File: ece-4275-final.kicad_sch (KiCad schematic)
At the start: 0 parts

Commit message: add esp32-s3
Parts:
- added U1: ESP32-S3, Package_DFN_QFN:QFN-56-1EP_7x7mm_P0.4mm_EP4x4mm, symbol MCU_Espressif:ESP32-S3
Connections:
- new net: U1.2 (VDD3P3), U1.3 (VDD3P3)
- new net: U1.55 (VDDA), U1.56 (VDDA)
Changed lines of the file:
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@@
 	(generator_version "10.0")
 	(paper "A4")
+	(symbol
+		(lib_id "MCU_Espressif:ESP32-S3")
+		(at 144.78 90.17 0)
+		(unit 1)
+		(body_style 1)
+		(exclude_from_sim no)
+		(in_bom yes)
+		(on_board yes)
+		(in_pos_files yes)
+		(dnp no)
+		(fields_autoplaced yes)
+		(property "Reference" "U1"
+			(at 146.9233 128.27 0)
+			(show_name no)
+			(do_not_autoplace no)
+			(effects
+				(font
+					(size 1.27 1.27)
+				)
+				(justify left)
+			)
+		)
+		(property "Value" "ESP32-S3"
+			(at 146.9233 130.81 0)
+			(show_name no)
+			(do_not_autoplace no)
+			(effects
+				(font
+					(size 1.27 1.27)
+				)
+				(justify left)
+			)
+		)
+		(property "Footprint" "Package_DFN_QFN:QFN-56-1EP_7x7mm_P0.4mm_EP4x4mm"
+			(at 144.78 138.43 0)
+			(hide yes)
+			(show_name no)
+			(do_not_autoplace no)
+			(effects
+				(font
+					(size 1.27 1.27)
+				)
+			)
+		)
+		(property "Datasheet" "https://www.espressif.com/sites/default/files/documentation/esp32-s3_datasheet_en.pdf"
+			(at 144.78 90.17 0)
+			(hide yes)
+			(show_name no)
+			(do_not_autoplace no)
+			(effects
+				(font
+					(size 1.27 1.27)
+				)
+			)
+		)
+		(property "Description" "Microcontroller, Wi-Fi 802.11b/g/n, Bluetooth, 32bit"
+			(at 144.78 90.17 0)
+			(hide yes)
+			(show_name no)
+			(do_not_autoplace no)
+			(effects
+				(font
+					(size 1.27 1.27)
+				)
+			)
+		)
+		(pin "57"
+		)
+		(pin "55"
+		)
+		(pin "54"
+		)
+		(pin "53"
+		)
+		(pin "52"
+		)
+		(pin "50"
+		)
+		(pin "49"
+		)
+		(pin "48"
+		)
+		(pin "47"
+		)
+		(pin "46"
+		)
+		(pin "44"
+		)
+		(pin "43"
+		)
+		(pin "42"
+		)
+		(pin "41"
+		)
+		(pin "40"
+		)
+		(pin "39"
+		)
+		(pin "38"
+		)
+		(pin "37"
+		)
+		(pin "35"
+		)
+		(pin "34"
+		)
+		(pin "27"
+		)
+		(pin "28"
+		)
+		(pin "29"
+		)
+		(pin "30"
+		)
+		(pin "31"
+		)
+		(pin "32"
+		)
+		(pin "33"
+		)
+		(pin "4"
+		)
+		(pin "5"
+		)
+		(pin "6"
+		)
+		(pin "7"
+		)
+		(pin "8"
+		)
+		(pin "9"
+		)
+		(pin "10"
+		)
+		(pin "11"
+		)
+		(pin "12"
+		)
+		(pin "13"
+		)
+		(pin "14"
+		)
+		(pin "15"
+		)
+		(pin "16"
+		)
+		(pin "17"
+		)
+		(pin "18"
+		)
+		(pin "19"
+		)
+		(pin "20"
+		)
+		(pin "21"
+		)
+		(pin "22"
+		)
+		(pin "23"
+		)
+		(pin "24"
+		)
+		(pin "25"
+		)
+		(pin "26"
+		)
+		(pin "1"
+		)
+		(pin "2"
+		)
+		(pin "3"
+		)
+		(pin "36"
+		)
+		(pin "45"
+		)
+		(pin "51"
+		)
+		(pin "56"
+		)
+		(instances
+			(project "ece-4275-final"
+				(path "/0c77f2af-cddb-472c-9a1b-8caed066380b"
+					(reference "U1")
+					(unit 1)
+				)
+			)
+		)
+	)
 	(sheet_instances
 		(path "/"

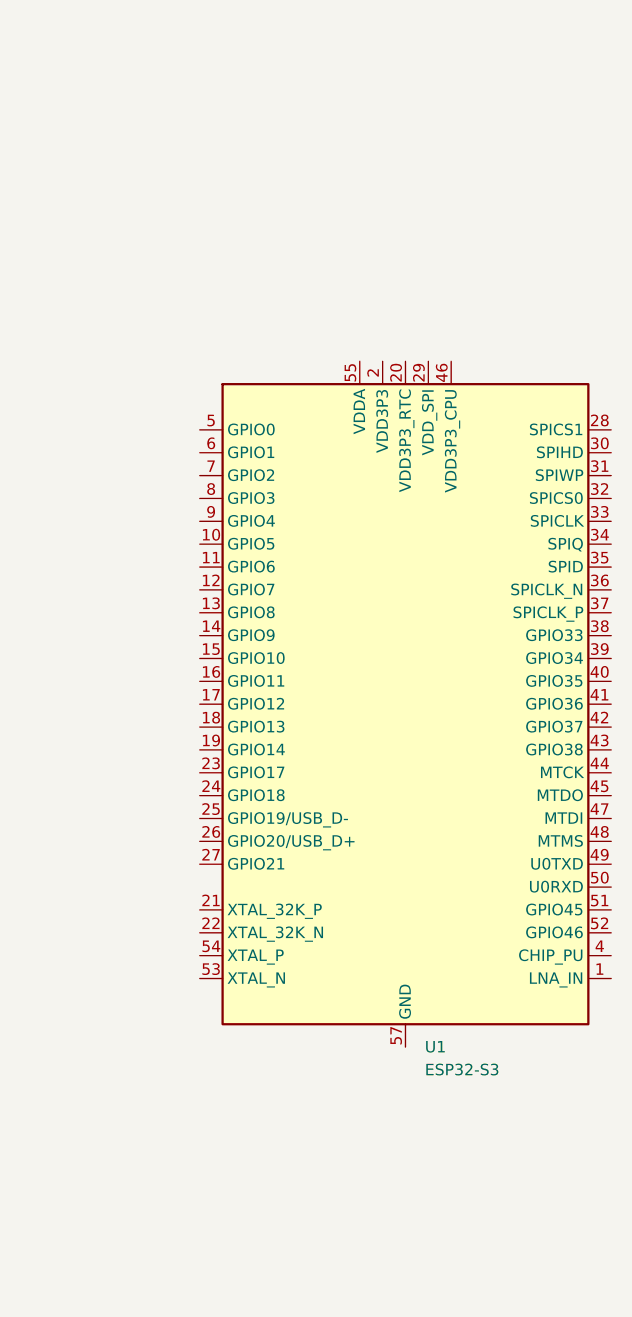
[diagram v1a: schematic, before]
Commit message: add dc step down
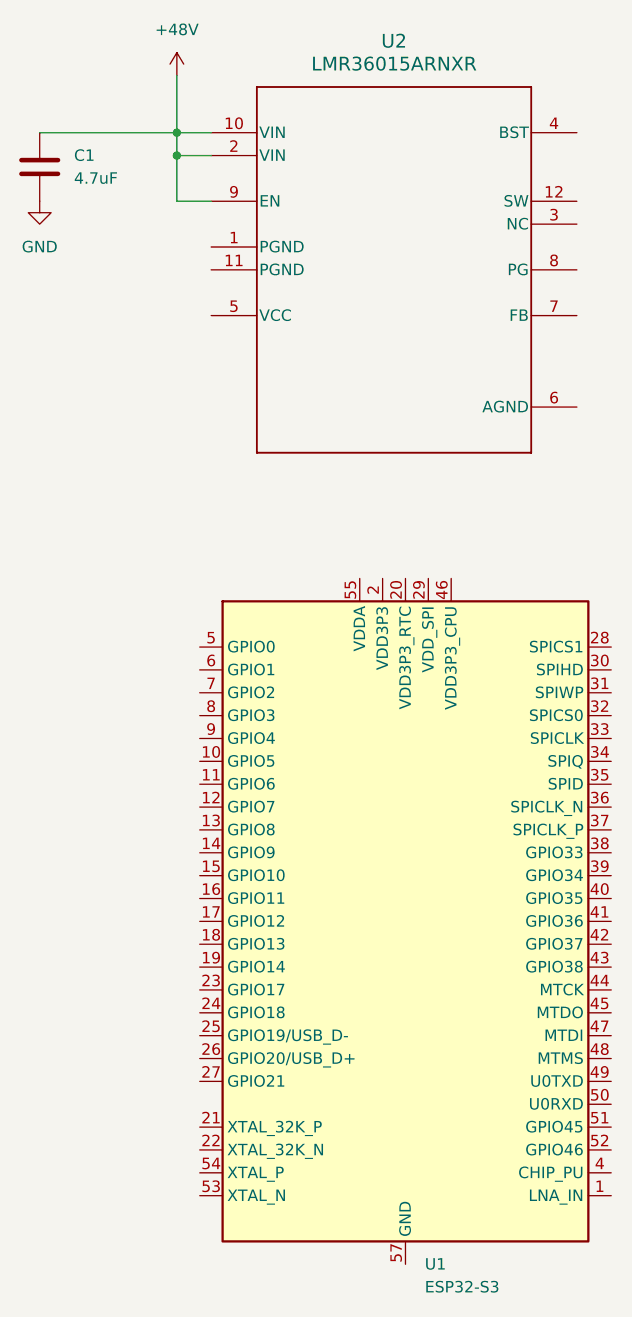
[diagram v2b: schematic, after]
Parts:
- added C1: 4.7uF, symbol Device:C
- added U2: LMR36015ARNXR, RNX0012B, symbol 2026-04-16_22-04-10:LMR36015ARNXR
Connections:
- new net +48V: C1.1, U2.10 (VIN), U2.2 (VIN), U2.9 (EN)
- new net GND: C1.2
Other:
- moved on the sheet: U1

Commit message: add library for local imports
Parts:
- removed U2: LMR36015ARNXR, RNX0012B, symbol 2026-04-16_22-04-10:LMR36015ARNXR
- added U2: LMR36015ARNXR, IMPORTS:LMR36015, symbol IMPORTS:LMR36015ARNXR
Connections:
- net +48V: now also U2.10 (VIN), U2.2 (VIN), U2.9 (EN)
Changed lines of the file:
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@@
-	)
-	(symbol
-		(lib_id "2026-04-16_22-04-10:LMR36015ARNXR")
-		(at 143.51 41.91 0)
-		(unit 1)
-		(body_style 1)
-		(exclude_from_sim no)
-		(in_bom yes)
-		(on_board yes)
-		(in_pos_files yes)
-		(dnp no)
-		(fields_autoplaced yes)
-		(property "Reference" "U2"
-			(at 143.51 16.51 0)
-			(show_name no)
-			(do_not_autoplace no)
-			(effects
-				(font
-					(size 1.524 1.524)
-				)
-			)
-		)
-		(property "Value" "LMR36015ARNXR"
-			(at 143.51 19.05 0)
-			(show_name no)
-			(do_not_autoplace no)
-			(effects
-				(font
-					(size 1.524 1.524)
-				)
-			)
-		)
-		(property "Footprint" "RNX0012B"
-			(at 143.51 41.91 0)
-			(hide yes)
-			(show_name no)
-			(do_not_autoplace no)
-			(effects
-				(font
-					(size 1.27 1.27)
-					(italic yes)
-				)
-			)
-		)
-		(property "Datasheet" "https://www.ti.com/lit/gpn/lmr36015"
-			(at 143.51 41.91 0)
-			(hide yes)
-			(show_name no)
-			(do_not_autoplace no)
-			(effects
-				(font
-					(size 1.27 1.27)
-					(italic yes)
-				)
-			)
-		)
-		(property "Description" ""
-			(at 143.51 41.91 0)
-			(hide yes)
-			(show_name no)
-			(do_not_autoplace no)
-			(effects
-				(font
-					(size 1.27 1.27)
-				)
-			)
-		)
-		(pin "2"
-		)
-		(pin "1"
-		)
-		(pin "12"
-		)
-		(pin "11"
-		)
-		(pin "10"
-		)
-		(pin "9"
-		)
-		(pin "8"
-		)
-		(pin "7"
-		)
-		(pin "6"
-		)
-		(pin "5"
-		)
-		(pin "4"
-		)
-		(pin "3"
-		)
-		(instances
-			(project "ece-4275-final"
-				(path "/0c77f2af-cddb-472c-9a1b-8caed066380b"
-					(reference "U2")
-					(unit 1)
-				)
-			)
-		)
 	)
 	(symbol
@@
 					(unit 1)
 				)
+			)
+		)
+	)
+	(symbol
+		(lib_id "IMPORTS:LMR36015ARNXR")
+		(at 143.51 41.91 0)
+		(unit 1)
+		(body_style 1)
+		(exclude_from_sim no)
+		(in_bom yes)
+		(on_board yes)
+		(in_pos_files yes)
+		(dnp no)
+		(fields_autoplaced yes)
+		(property "Reference" "U2"
+			(at 143.51 16.51 0)
+			(show_name no)
+			(do_not_autoplace no)
+			(effects
+				(font
+					(size 1.524 1.524)
+				)
+			)
+		)
+		(property "Value" "LMR36015ARNXR"
+			(at 143.51 19.05 0)
+			(show_name no)
+			(do_not_autoplace no)
+			(effects
+				(font
+					(size 1.524 1.524)
+				)
+			)
+		)
+		(property "Footprint" "IMPORTS:LMR36015"
+			(at 143.51 41.91 0)
+			(hide yes)
+			(show_name no)
+			(do_not_autoplace no)
+			(effects
+				(font
+					(size 1.27 1.27)
+					(italic yes)
+				)
+			)
+		)
+		(property "Datasheet" "https://www.ti.com/lit/gpn/lmr36015"
+			(at 143.51 41.91 0)
+			(hide yes)
+			(show_name no)
+			(do_not_autoplace no)
+			(effects
+				(font
+					(size 1.27 1.27)
+					(italic yes)
+				)
+			)
+		)
+		(property "Description" ""
+			(at 143.51 41.91 0)
+			(hide yes)
+			(show_name no)
+			(do_not_autoplace no)
+			(effects
+				(font
+					(size 1.27 1.27)
+				)
+			)
+		)
+		(pin "6"
+		)
+		(pin "5"
+		)
+		(pin "2"
+		)
+		(pin "4"
+		)
+		(pin "1"
+		)
+		(pin "3"
+		)
+		(pin "11"
+		)
+		(pin "10"
+		)
+		(pin "12"
+		)
+		(pin "9"
+		)
+		(pin "8"
+		)
+		(pin "7"
+		)
+		(instances
+			(project "ece-4275-final"
+				(path "/0c77f2af-cddb-472c-9a1b-8caed066380b"
+					(reference "U2")
+					(unit 1)
+				)

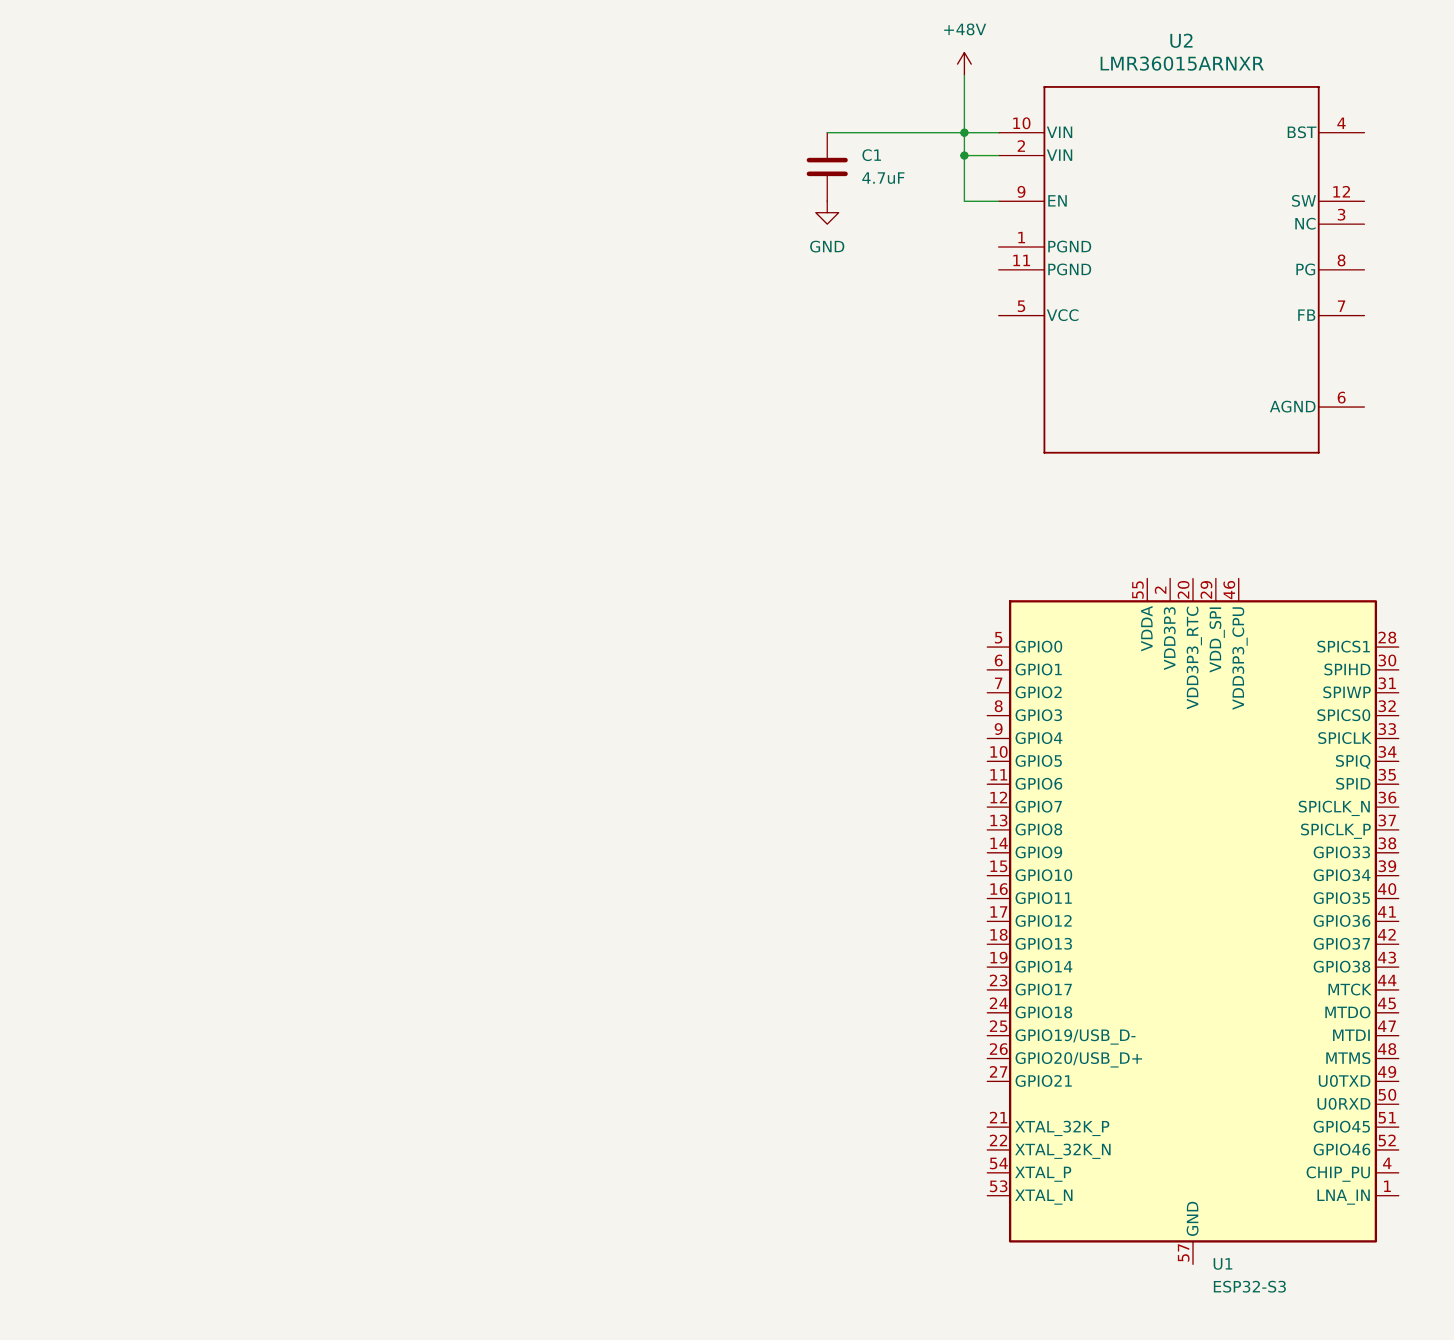
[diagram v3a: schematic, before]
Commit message: add DCDC converter + LDO
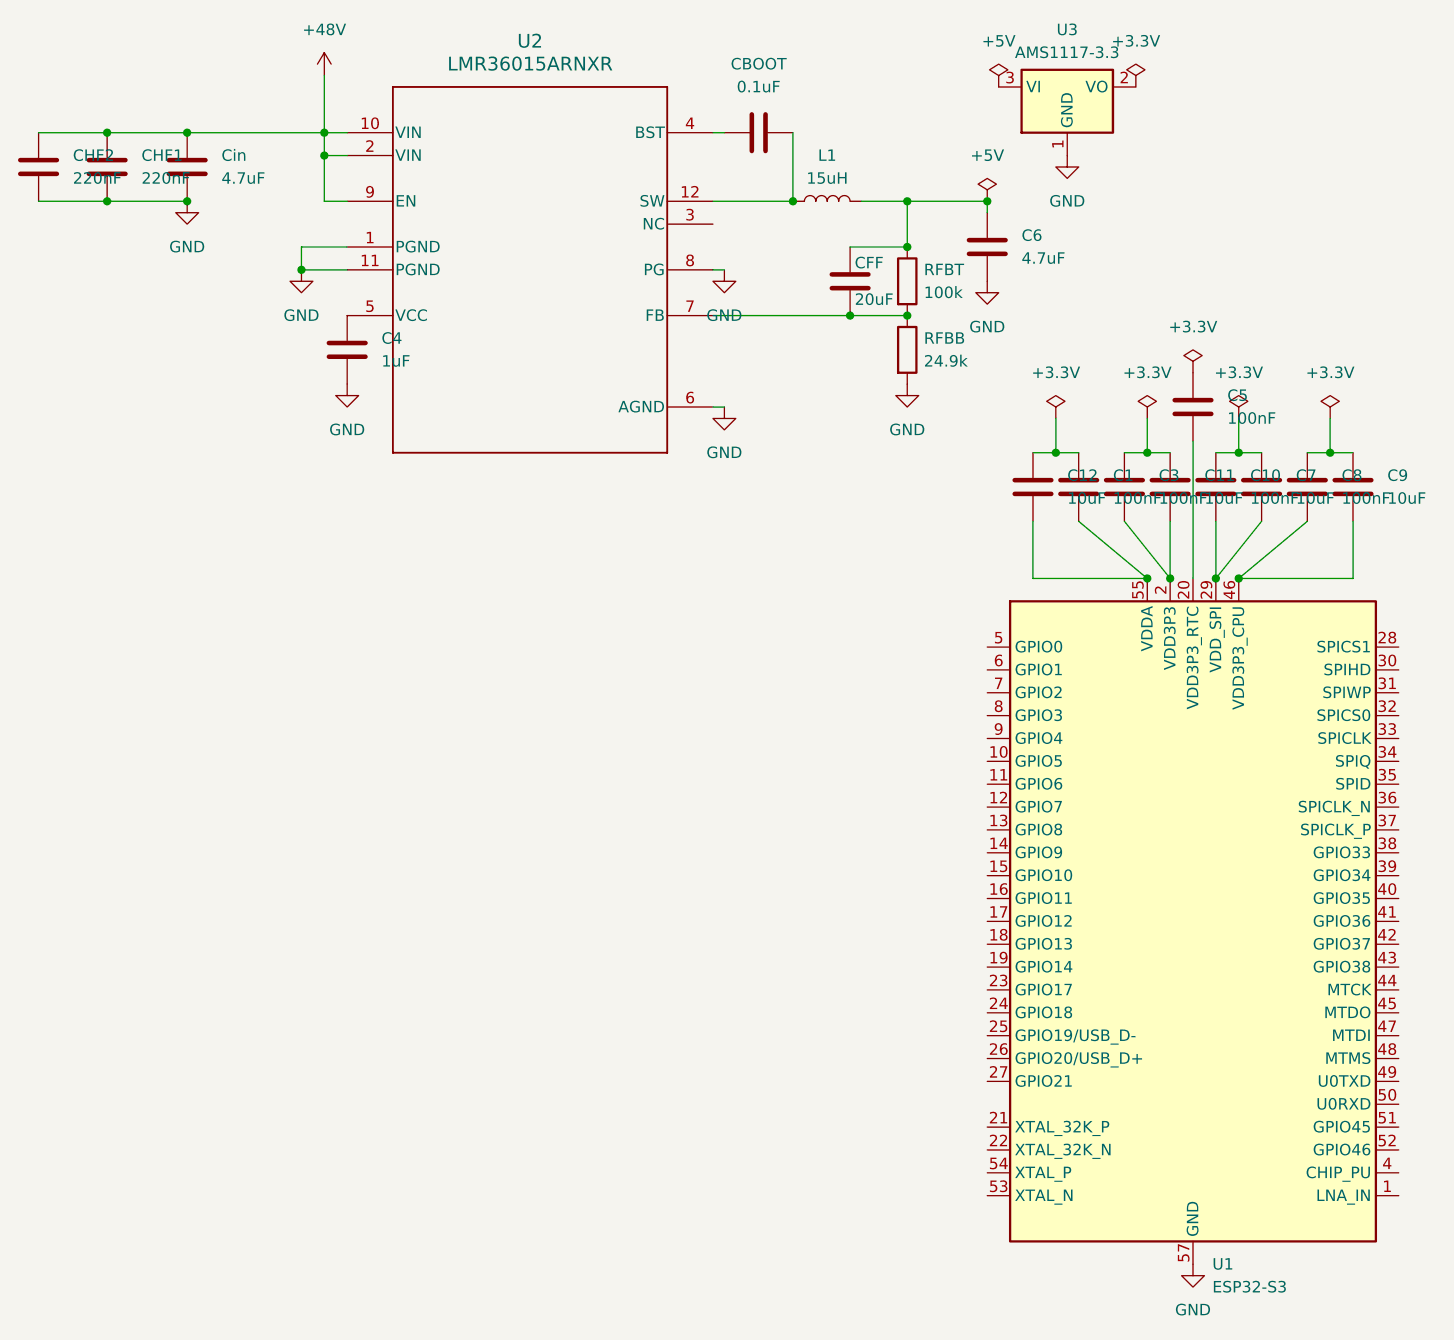
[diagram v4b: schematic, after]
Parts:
- added C1, C10, C3, C5, C8: 100nF, symbol Device:C
- added C11, C12, C7, C9: 10uF, symbol Device:C
- added C4: 1uF, Capacitor_SMD:C_0402_1005Metric, symbol Device:C
- added C6: 4.7uF, Capacitor_SMD:C_0402_1005Metric, symbol Device:C
- added CBOOT: 0.1uF, Capacitor_SMD:C_0402_1005Metric, symbol Device:C
- added CFF: 20uF, Capacitor_SMD:C_0402_1005Metric, symbol Device:C
- added CHF1, CHF2: 220nF, Capacitor_SMD:C_0402_1005Metric, symbol Device:C
- added L1: 15uH, symbol Device:L
- added RFBB: 24.9k, symbol Device:R
- added RFBT: 100k, symbol Device:R
- added U3: AMS1117-3.3, Package_TO_SOT_SMD:SOT-223-3_TabPin2, symbol Regulator_Linear:AMS1117-3.3
- Cin: renamed from C1; footprint (none) -> Capacitor_SMD:C_0402_1005Metric
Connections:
- net +48V: now also CHF1.1, CHF2.1
- net GND: now also U1.57 (GND), U2.1 (PGND), U2.11 (PGND), U2.6 (AGND), U2.8 (PG), C4.2, C6.2, CHF1.2, CHF2.2, RFBB.2, U3.1 (GND)
- net at U1.2 (VDD3P3), U1.3 (VDD3P3): now also C11.2, C3.2
- net at U1.20 (VDD3P3_RTC): now also C5.2
- net at U1.29 (VDD_SPI): now also C10.2, C7.2
- net at U1.46 (VDD3P3_CPU): now also C8.2, C9.2
- net at U1.55 (VDDA), U1.56 (VDDA): now also C1.2, C12.2
- net at U2.12 (SW): now also CBOOT.2, L1.1
- net at U2.4 (BST): now also CBOOT.1
- net at U2.5 (VCC): now also C4.1
- net at U2.7 (FB): now also CFF.2, RFBB.1, RFBT.2
- new net: C11.1, C3.1
- new net: C8.1, C9.1
- new net: C1.1, C12.1
- new net: C6.1, CFF.1, L1.2, RFBT.1
- new net: C10.1, C7.1
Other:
- moved on the sheet: Cin, U2
